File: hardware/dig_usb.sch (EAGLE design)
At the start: 201 parts, among them IC101 AT90USB1287-AU, IC102 MAX487CSA, IC103 74HC166D, IC301 LTV-356T, IC302 LTV-356T, IC303 LTV-356T, IC304 LTV-356T, IC305 LTV-356T, IC306 LTV-356T, IC307 LTV-356T, IC308 LTV-356T, IC401 DS1337S, K401 S202S02, K402 S202S02, K403 S202S02, K404 S202S02, K405 S202S02, K406 S202S02, K407 S202S02, K408 S202S02, Q101 16MHz, Q301 BCR191, Q302 BCR191, Q303 BCR191, Q304 BCR191, Q305 BCR191, Q306 BCR191, Q307 BCR191, Q308 BCR191, Q401 32,768kHz, X102 ISP, X301 AKL_230-02, X302 RIA-73-02, X304 RIA-73-02, X305 RIA-73-02, X306 RIA-73-02, X307 RIA-73-02, X308 AKL_230-08, X401 RIA-73-02, X402 RIA-73-02, X403 AKL_230-04, X406 AKL_230-08, X407 RIA-73-02, X408 RIA-73-02, X409 AKL_230-02, X410 RIA-73-02, X411 RIA-73-02, X412 RIA-73-02

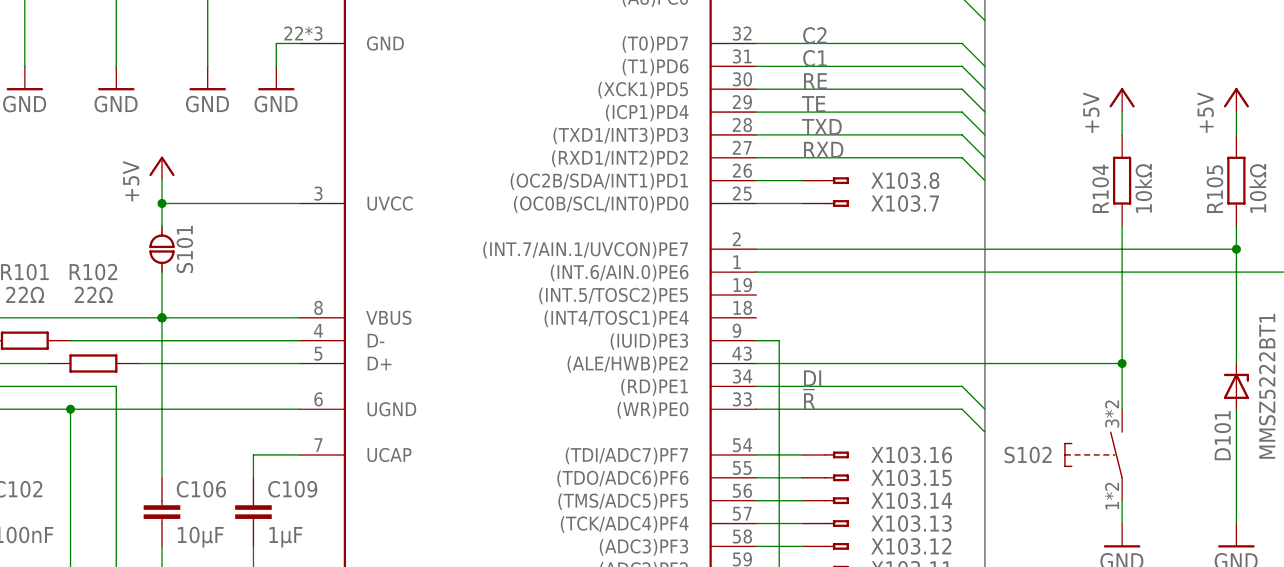
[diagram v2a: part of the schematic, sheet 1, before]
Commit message: Zusätzlicher Kondensator für UVcc; HWB mit INT4 verbunden
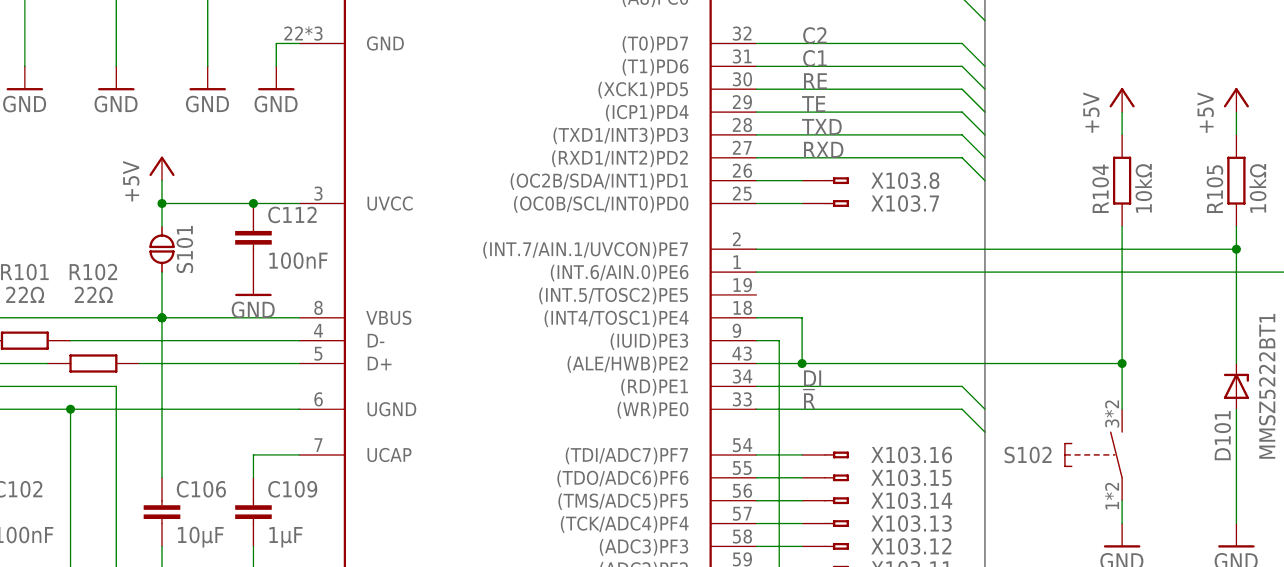
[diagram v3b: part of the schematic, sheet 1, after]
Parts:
- added C112: 100nF, passiv:C_0603
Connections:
- net +5V: now also C112.1
- net GND: now also C112.2
- net N$147: now also IC101.(INT4/TOSC1)PE4
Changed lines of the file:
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@@
 <part name="0V" library="test" deviceset="TEST" device="_VIA_08"/>
 <part name="5V" library="test" deviceset="TEST" device="_VIA_08"/>
+<part name="C112" library="passiv" deviceset="C_" device="0603" value="100nF"/>
+<part name="GND5" library="versorgung" deviceset="GND" device=""/>
 </parts>
 <sheets>
@@
 <instance part="P+103" gate="1" x="45.72" y="76.2"/>
 <instance part="GND105" gate="1" x="35.56" y="27.94"/>
+<instance part="C112" gate="G$1" x="55.88" y="68.58"/>
+<instance part="GND5" gate="1" x="55.88" y="60.96"/>
 </instances>
 <busses>
@@
 <wire x1="152.4" y1="35.56" x2="152.4" y2="38.1" width="0.1524" layer="91"/>
 </segment>
+<segment>
+<pinref part="C112" gate="G$1" pin="2"/>
+<pinref part="GND5" gate="1" pin="GND"/>
+</segment>
 </net>
 <net name="+5V" class="0">
@@
 <pinref part="IC101" gate="G$1" pin="UVCC"/>
 <pinref part="P+103" gate="1" pin="+5V"/>
-<wire x1="60.96" y1="71.12" x2="45.72" y2="71.12" width="0.1524" layer="91"/>
+<wire x1="60.96" y1="71.12" x2="55.88" y2="71.12" width="0.1524" layer="91"/>
+<wire x1="55.88" y1="71.12" x2="45.72" y2="71.12" width="0.1524" layer="91"/>
 <wire x1="45.72" y1="71.12" x2="45.72" y2="73.66" width="0.1524" layer="91"/>
 <wire x1="45.72" y1="68.58" x2="45.72" y2="71.12" width="0.1524" layer="91"/>
 <junction x="45.72" y="71.12"/>
+<pinref part="C112" gate="G$1" pin="1"/>
+<junction x="55.88" y="71.12"/>
 </segment>
 </net>
@@
 <pinref part="IC101" gate="G$1" pin="(ALE/HWB)PE2"/>
 <pinref part="S102" gate="G$1" pin="S"/>
-<wire x1="111.76" y1="53.34" x2="152.4" y2="53.34" width="0.1524" layer="91"/>
+<wire x1="111.76" y1="53.34" x2="116.84" y2="53.34" width="0.1524" layer="91"/>
+<wire x1="116.84" y1="53.34" x2="152.4" y2="53.34" width="0.1524" layer="91"/>
 <wire x1="152.4" y1="53.34" x2="152.4" y2="48.26" width="0.1524" layer="91"/>
 <pinref part="R104" gate="G$1" pin="1"/>
 <wire x1="152.4" y1="68.58" x2="152.4" y2="53.34" width="0.1524" layer="91"/>
 <junction x="152.4" y="53.34"/>
-</segment>
-</net>
+<pinref part="IC101" gate="G$1" pin="(INT4/TOSC1)PE4"/>
+<wire x1="111.76" y1="58.42" x2="116.84" y2="58.42" width="0.1524" layer="91"/>
+<wire x1="116.84" y1="58.42" x2="116.84" y2="53.34" width="0.1524" layer="91"/>
+<junction x="116.84" y="53.34"/>
+</segment>
+</net>

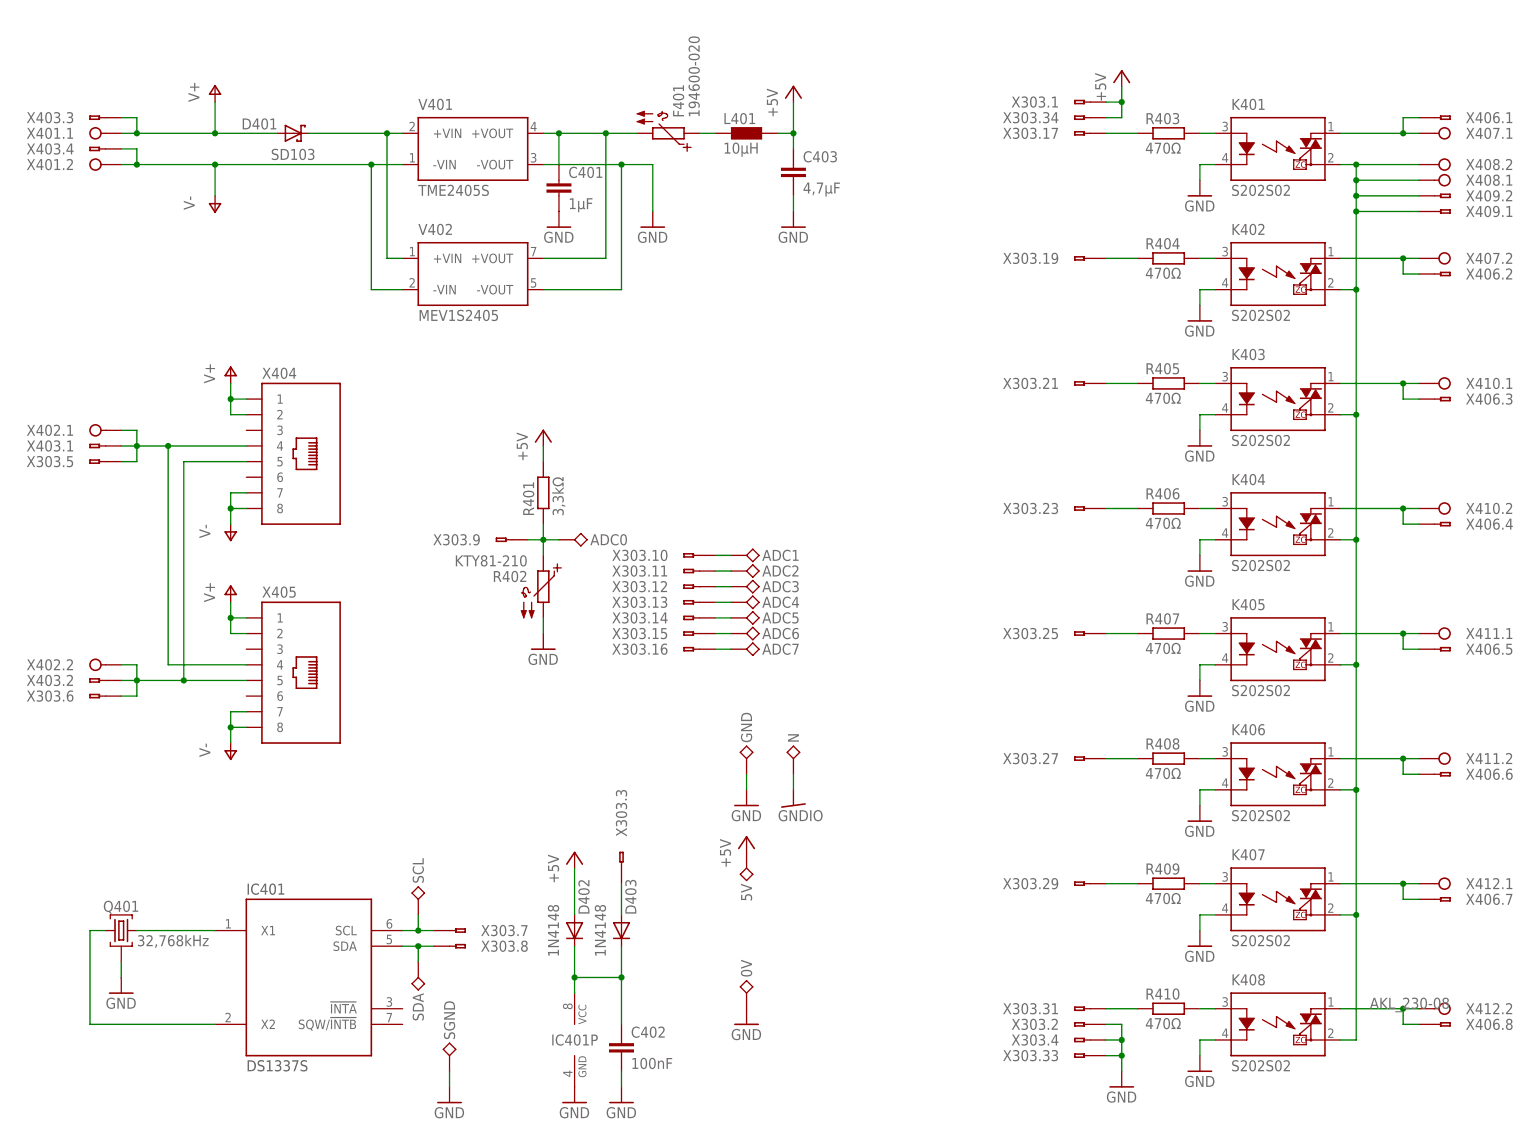
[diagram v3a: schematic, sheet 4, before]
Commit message: I2C EEPROM hinzugefügt auf dig_usb hinzugefügt
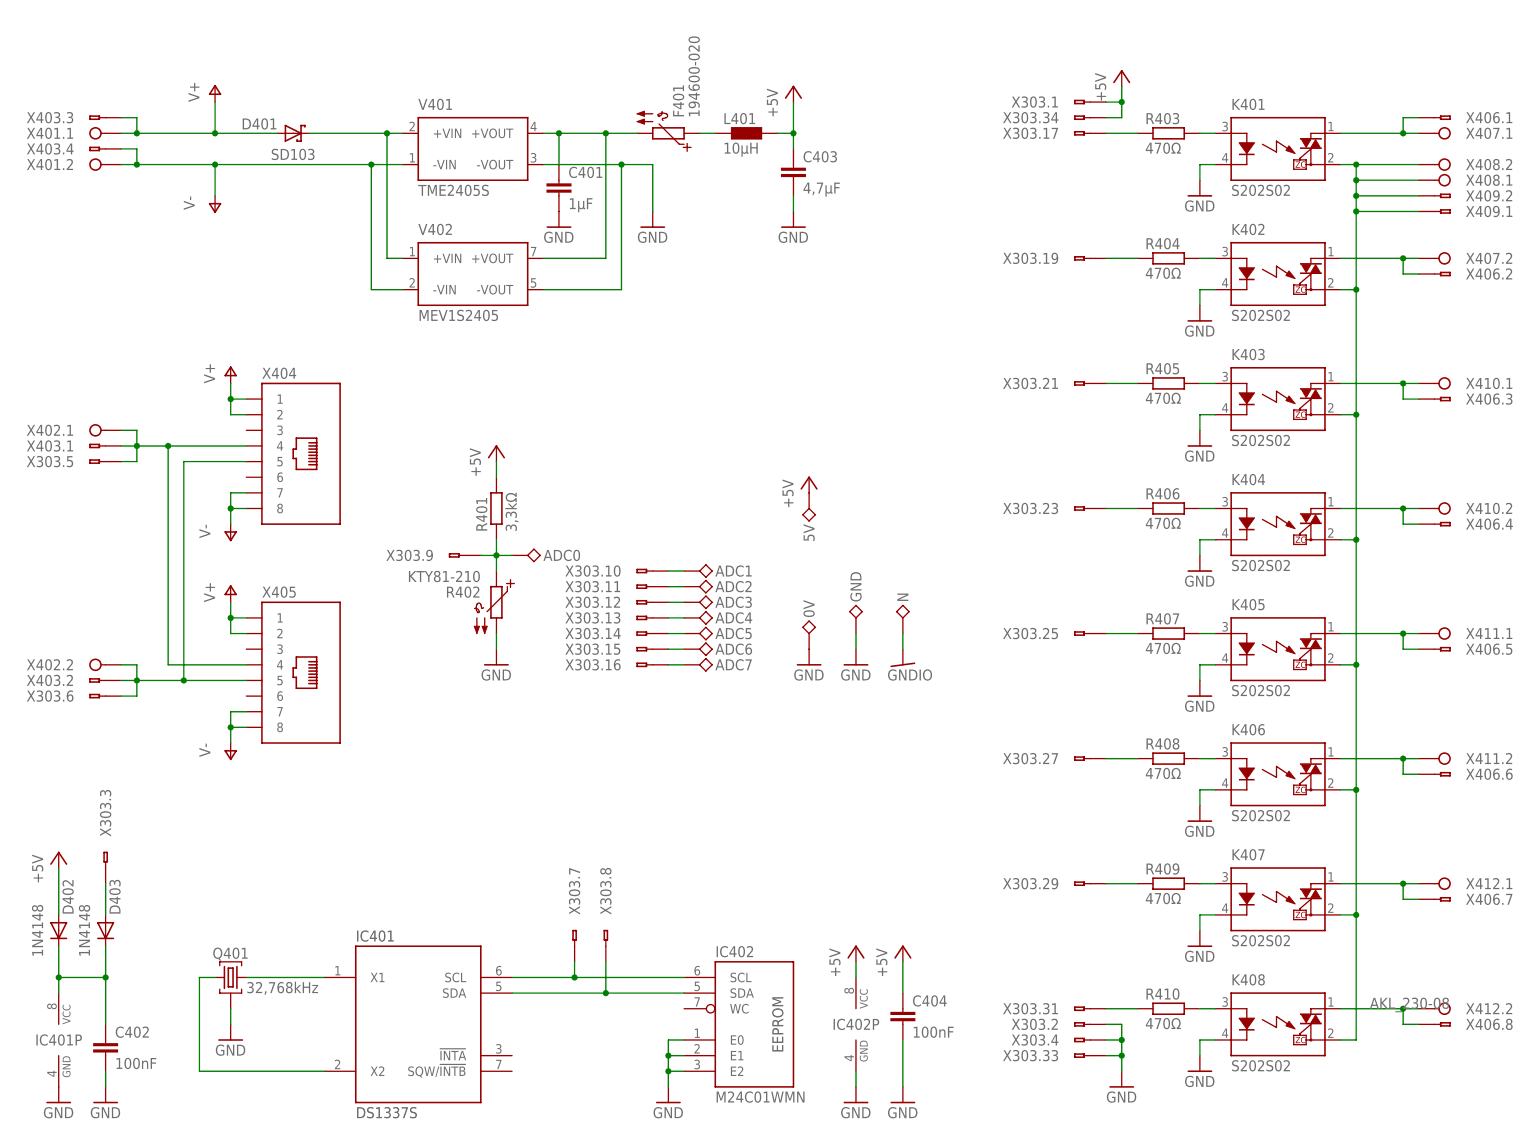
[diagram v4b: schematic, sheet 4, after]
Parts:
- removed SCL, SDA, SGND: (no value), test:TEST_VIA_06
- added C404: 100nF, passiv:C_0603
- added IC402: M24C01WMN, ic-speicher:M24C01WMN
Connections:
- net +5V: now also C404.1, IC402P.VCC
- net GND: now also C404.2, IC402G$1.E0, IC402G$1.E1, IC402G$1.E2, IC402P.GND; no longer SGND.1
- net N$131: now also IC402G$1.SCL; no longer SCL.1
- net N$132: now also IC402G$1.SDA; no longer SDA.1
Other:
- moved on the sheet: 0V, 5V, ADC0, ADC1, ADC2, ADC3, ADC4, ADC5, ADC6, ADC7, C402, D402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
